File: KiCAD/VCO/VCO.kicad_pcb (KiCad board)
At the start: 4 copper layers, 215 x 85 mm, 40 parts, among them J1 CV IN 1, J2 CV IN 2, J3 PWM, J4 SAW OUT, J5 PULSE OUT, J6 Conn_01x03_Pin, J7 Conn_01x03_Pin, Q1 NPN, T1 PNP, T2 NPN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

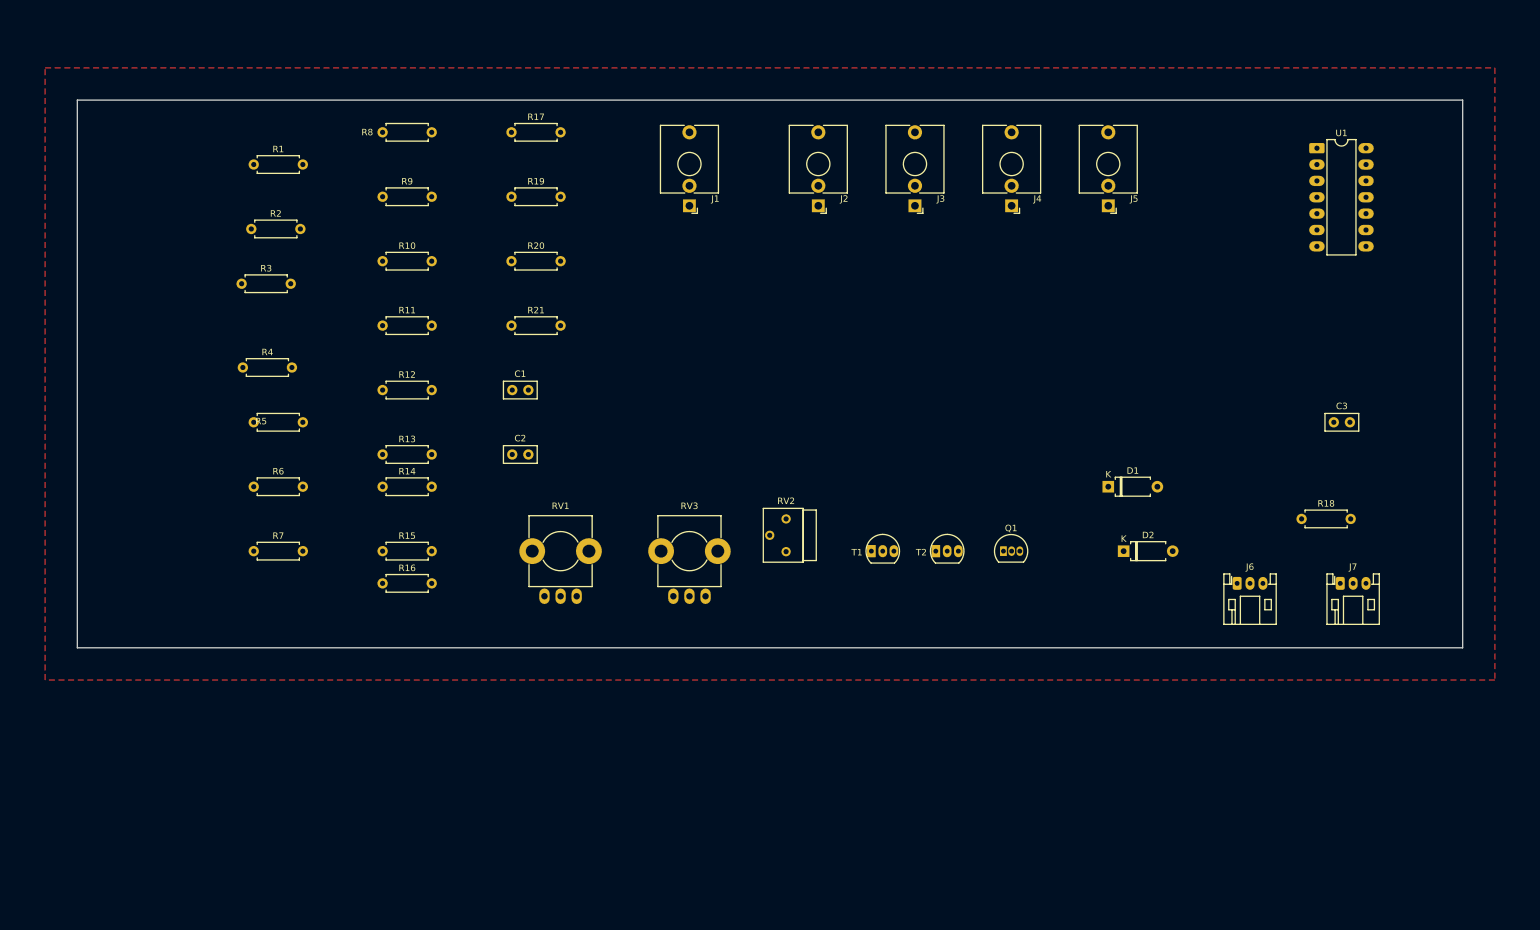
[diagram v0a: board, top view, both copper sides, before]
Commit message: VCO Board Setup
Set up net classes and removed additional layers
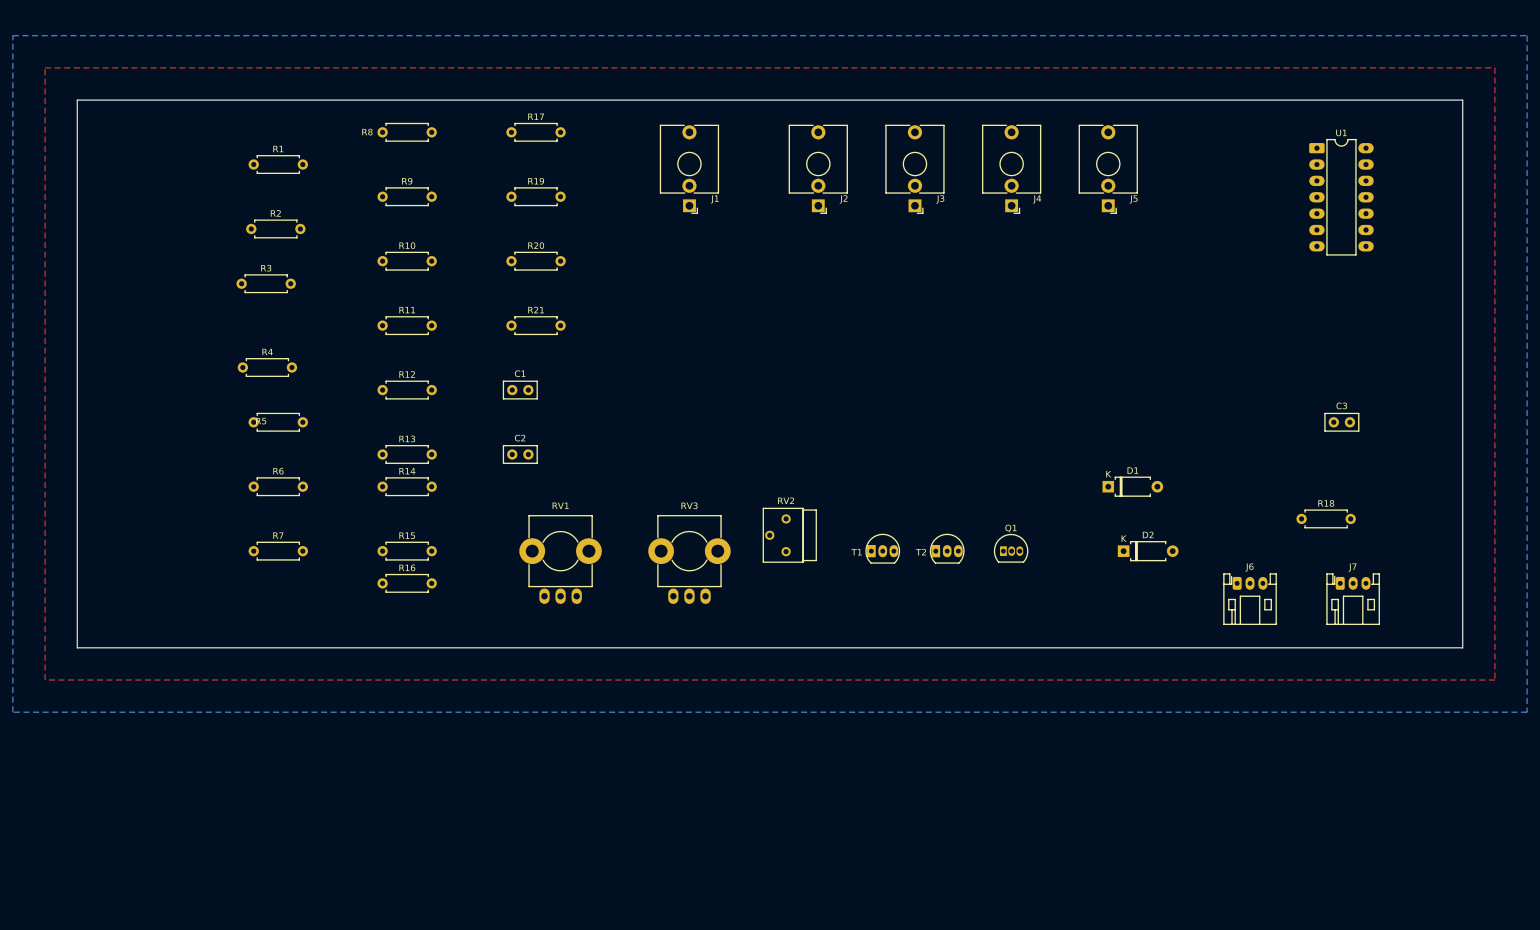
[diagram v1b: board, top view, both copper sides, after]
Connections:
- U1 pad 14: (no net) -> VDD
- U1 pad 7: (no net) -> VSS
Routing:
- added copper zone on B.Cu, net VDD
- removed copper zone on In1.Cu, net VDD
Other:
- copper layers 4 -> 2
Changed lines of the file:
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@@
 	(layers
 		(0 "F.Cu" signal)
-		(4 "In1.Cu" signal)
-		(6 "In2.Cu" signal)
 		(2 "B.Cu" signal)
 		(9 "F.Adhes" user "F.Adhesive")
@@
 			)
 			(layer "dielectric 1"
-				(type "prepreg")
-				(thickness 0.1)
-				(material "FR4")
-				(epsilon_r 4.5)
-				(loss_tangent 0.02)
-			)
-			(layer "In1.Cu"
-				(type "copper")
-				(thickness 0.035)
-			)
-			(layer "dielectric 2"
 				(type "core")
-				(thickness 1.24)
-				(material "FR4")
-				(epsilon_r 4.5)
-				(loss_tangent 0.02)
-			)
-			(layer "In2.Cu"
-				(type "copper")
-				(thickness 0.035)
-			)
-			(layer "dielectric 3"
-				(type "prepreg")
-				(thickness 0.1)
+				(thickness 1.51)
 				(material "FR4")
 				(epsilon_r 4.5)
@@
 			(psa4output no)
 			(plot_black_and_white yes)
-			(plotinvisibletext no)
 			(sketchpadsonfab no)
 			(plotpadnumbers no)
@@
 			(net 0)
 			(net_name "")
-			(layers "F.Cu" "In1.Cu" "In2.Cu")
+			(layer "F.Cu")
 			(hatch full 0.508)
 			(connect_pads
@@
 			(net 0)
 			(net_name "")
-			(layers "F.Cu" "In1.Cu" "In2.Cu")
+			(layer "F.Cu")
 			(hatch full 0.508)
 			(connect_pads
@@
 			(layers "*.Cu" "*.Mask")
 			(remove_unused_layers no)
+			(net 27 "VSS")
 		)
 		(pad "8" thru_hole oval
@@
 			(layers "*.Cu" "*.Mask")
 			(remove_unused_layers no)
+			(net 17 "VDD")
 		)
 		(embedded_fonts no)
@@
 			(net 0)
 			(net_name "")
-			(layers "F.Cu" "In1.Cu" "In2.Cu")
+			(layer "F.Cu")
 			(hatch full 0.508)
 			(connect_pads
@@
 			(net 0)
 			(net_name "")
-			(layers "F.Cu" "In1.Cu" "In2.Cu")
+			(layer "F.Cu")
 			(hatch full 0.508)
 			(connect_pads
@@
 			(net 0)
 			(net_name "")
-			(layers "F.Cu" "In1.Cu" "In2.Cu")
+			(layer "F.Cu")
 			(hatch full 0.508)
 			(connect_pads
@@
 		(net 17)
 		(net_name "VDD")
-		(layer "In1.Cu")
+		(layer "B.Cu")
 		(hatch edge 0.5)
 		(priority 1)

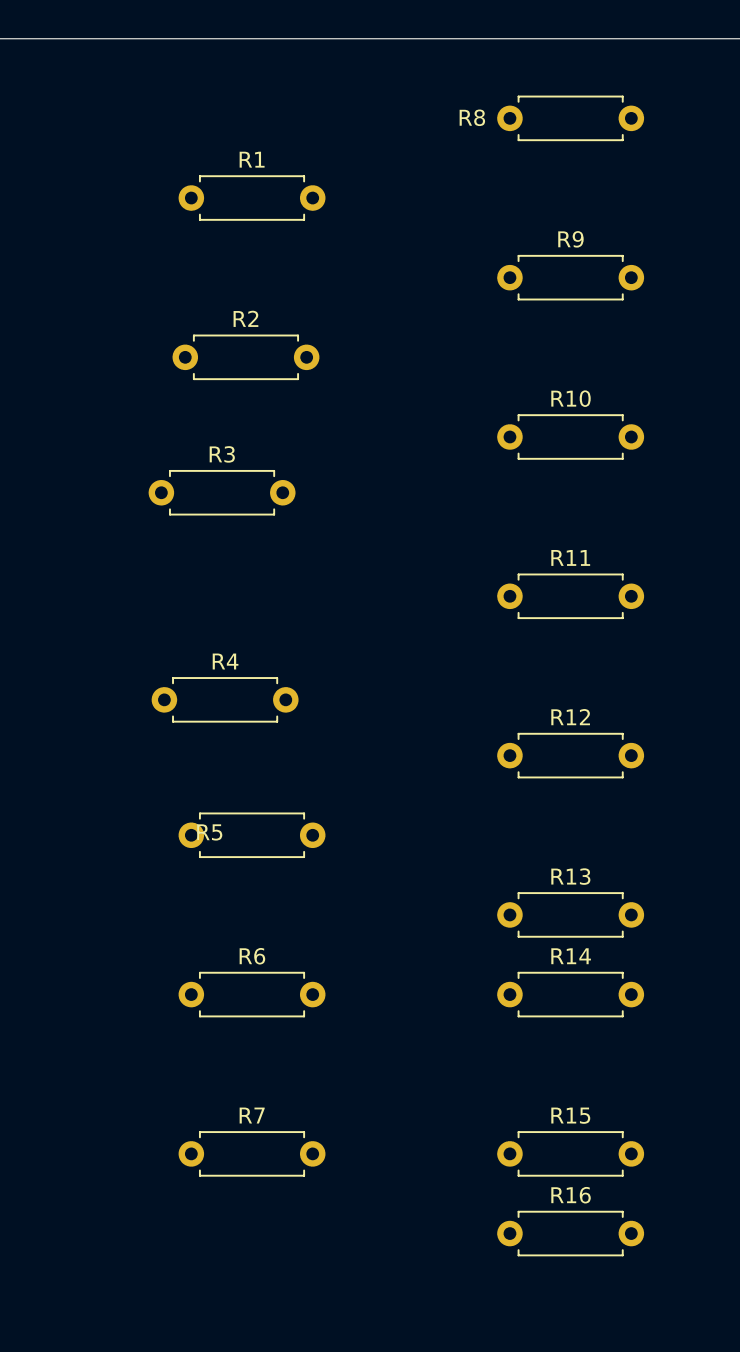
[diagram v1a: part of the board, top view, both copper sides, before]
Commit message: VCO PCB Resistor alignment.
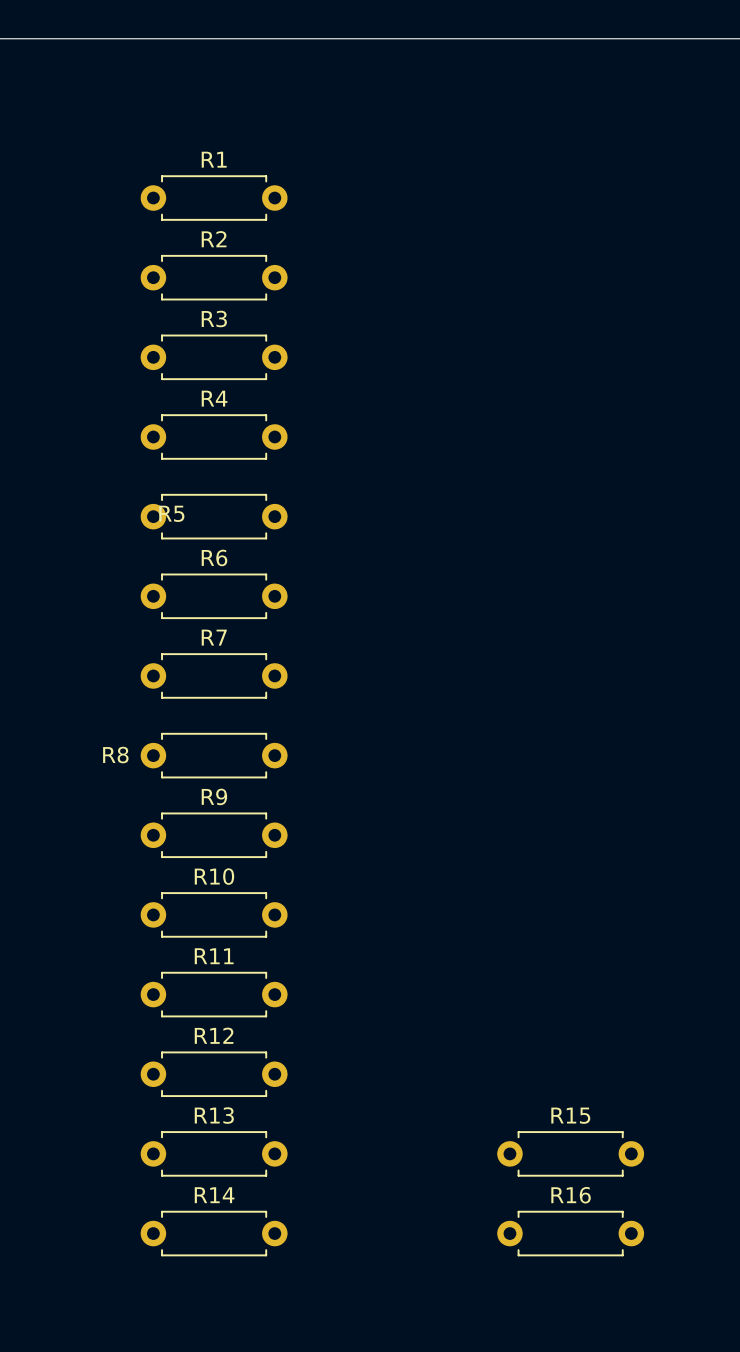
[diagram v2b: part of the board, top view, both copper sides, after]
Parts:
- moved R8 45.8 mm to (60.0, 85.0)
- moved R9 41.5 mm to (60.0, 90.0)
- moved R10 37.4 mm to (60.0, 95.0)
- moved R11 33.6 mm to (60.0, 100.0)
- moved R7 30.1 mm to (60.0, 80.0)
- moved R12 30.0 mm to (60.0, 105.0)
- moved R13 26.9 mm to (60.0, 110.0)
- moved R14 26.9 mm to (60.0, 115.0)
- moved R6 25.1 mm to (60.0, 75.0)
- moved R5 20.1 mm to (60.0, 70.0)
- moved R4 16.5 mm to (60.0, 65.0)
- moved R3 8.51 mm to (60.0, 60.0)
- moved R2 5.39 mm to (60.0, 55.0)
- moved R1 2.38 mm to (60.0, 50.0)
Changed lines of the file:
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@@
 	(footprint "Resistor_THT:R_Axial_DIN0207_L6.3mm_D2.5mm_P7.62mm_Horizontal"
 		(layer "F.Cu")
-		(at 62.38 110)
+		(at 60 80)
 		(descr "Resistor, Axial_DIN0207 series, Axial, Horizontal, pin pitch=7.62mm, 0.25W = 1/4W, length*diameter=6.3*2.5mm^2, http://cdn-reichelt.de/documents/datenblatt/B400/1_4W%23YAG.pdf")
 		(tags "Resistor Axial_DIN0207 series Axial Horizontal pin pitch 7.62mm 0.25W = 1/4W length 6.3mm diameter 2.5mm")
@@
 	(footprint "Resistor_THT:R_Axial_DIN0207_L6.3mm_D2.5mm_P7.62mm_Horizontal"
 		(layer "F.Cu")
-		(at 60.5 68.5)
+		(at 60 60)
 		(descr "Resistor, Axial_DIN0207 series, Axial, Horizontal, pin pitch=7.62mm, 0.25W = 1/4W, length*diameter=6.3*2.5mm^2, http://cdn-reichelt.de/documents/datenblatt/B400/1_4W%23YAG.pdf")
 		(tags "Resistor Axial_DIN0207 series Axial Horizontal pin pitch 7.62mm 0.25W = 1/4W length 6.3mm diameter 2.5mm")
@@
 	(footprint "Resistor_THT:R_Axial_DIN0207_L6.3mm_D2.5mm_P7.62mm_Horizontal"
 		(layer "F.Cu")
-		(at 62.38 90)
+		(at 60 70)
 		(descr "Resistor, Axial_DIN0207 series, Axial, Horizontal, pin pitch=7.62mm, 0.25W = 1/4W, length*diameter=6.3*2.5mm^2, http://cdn-reichelt.de/documents/datenblatt/B400/1_4W%23YAG.pdf")
 		(tags "Resistor Axial_DIN0207 series Axial Horizontal pin pitch 7.62mm 0.25W = 1/4W length 6.3mm diameter 2.5mm")
@@
 	(footprint "Resistor_THT:R_Axial_DIN0207_L6.3mm_D2.5mm_P7.62mm_Horizontal"
 		(layer "F.Cu")
-		(at 82.38 75)
+		(at 60 100)
 		(descr "Resistor, Axial_DIN0207 series, Axial, Horizontal, pin pitch=7.62mm, 0.25W = 1/4W, length*diameter=6.3*2.5mm^2, http://cdn-reichelt.de/documents/datenblatt/B400/1_4W%23YAG.pdf")
 		(tags "Resistor Axial_DIN0207 series Axial Horizontal pin pitch 7.62mm 0.25W = 1/4W length 6.3mm diameter 2.5mm")
@@
 	(footprint "Resistor_THT:R_Axial_DIN0207_L6.3mm_D2.5mm_P7.62mm_Horizontal"
 		(layer "F.Cu")
-		(at 82.38 85)
+		(at 60 105)
 		(descr "Resistor, Axial_DIN0207 series, Axial, Horizontal, pin pitch=7.62mm, 0.25W = 1/4W, length*diameter=6.3*2.5mm^2, http://cdn-reichelt.de/documents/datenblatt/B400/1_4W%23YAG.pdf")
 		(tags "Resistor Axial_DIN0207 series Axial Horizontal pin pitch 7.62mm 0.25W = 1/4W length 6.3mm diameter 2.5mm")
@@
 	(footprint "Resistor_THT:R_Axial_DIN0207_L6.3mm_D2.5mm_P7.62mm_Horizontal"
 		(layer "F.Cu")
-		(at 82.38 45)
+		(at 60 85)
 		(descr "Resistor, Axial_DIN0207 series, Axial, Horizontal, pin pitch=7.62mm, 0.25W = 1/4W, length*diameter=6.3*2.5mm^2, http://cdn-reichelt.de/documents/datenblatt/B400/1_4W%23YAG.pdf")
 		(tags "Resistor Axial_DIN0207 series Axial Horizontal pin pitch 7.62mm 0.25W = 1/4W length 6.3mm diameter 2.5mm")
@@
 	(footprint "Resistor_THT:R_Axial_DIN0207_L6.3mm_D2.5mm_P7.62mm_Horizontal"
 		(layer "F.Cu")
-		(at 82.38 95)
+		(at 60 110)
 		(descr "Resistor, Axial_DIN0207 series, Axial, Horizontal, pin pitch=7.62mm, 0.25W = 1/4W, length*diameter=6.3*2.5mm^2, http://cdn-reichelt.de/documents/datenblatt/B400/1_4W%23YAG.pdf")
 		(tags "Resistor Axial_DIN0207 series Axial Horizontal pin pitch 7.62mm 0.25W = 1/4W length 6.3mm diameter 2.5mm")
@@
 	(footprint "Resistor_THT:R_Axial_DIN0207_L6.3mm_D2.5mm_P7.62mm_Horizontal"
 		(layer "F.Cu")
-		(at 82.38 100)
+		(at 60 115)
 		(descr "Resistor, Axial_DIN0207 series, Axial, Horizontal, pin pitch=7.62mm, 0.25W = 1/4W, length*diameter=6.3*2.5mm^2, http://cdn-reichelt.de/documents/datenblatt/B400/1_4W%23YAG.pdf")
 		(tags "Resistor Axial_DIN0207 series Axial Horizontal pin pitch 7.62mm 0.25W = 1/4W length 6.3mm diameter 2.5mm")
@@
 	(footprint "Resistor_THT:R_Axial_DIN0207_L6.3mm_D2.5mm_P7.62mm_Horizontal"
 		(layer "F.Cu")
-		(at 62 60)
+		(at 60 55)
 		(descr "Resistor, Axial_DIN0207 series, Axial, Horizontal, pin pitch=7.62mm, 0.25W = 1/4W, length*diameter=6.3*2.5mm^2, http://cdn-reichelt.de/documents/datenblatt/B400/1_4W%23YAG.pdf")
 		(tags "Resistor Axial_DIN0207 series Axial Horizontal pin pitch 7.62mm 0.25W = 1/4W length 6.3mm diameter 2.5mm")
@@
 	(footprint "Resistor_THT:R_Axial_DIN0207_L6.3mm_D2.5mm_P7.62mm_Horizontal"
 		(layer "F.Cu")
-		(at 82.38 55)
+		(at 60 90)
 		(descr "Resistor, Axial_DIN0207 series, Axial, Horizontal, pin pitch=7.62mm, 0.25W = 1/4W, length*diameter=6.3*2.5mm^2, http://cdn-reichelt.de/documents/datenblatt/B400/1_4W%23YAG.pdf")
 		(tags "Resistor Axial_DIN0207 series Axial Horizontal pin pitch 7.62mm 0.25W = 1/4W length 6.3mm diameter 2.5mm")
@@
 	(footprint "Resistor_THT:R_Axial_DIN0207_L6.3mm_D2.5mm_P7.62mm_Horizontal"
 		(layer "F.Cu")
-		(at 60.69 81.5)
+		(at 60 65)
 		(descr "Resistor, Axial_DIN0207 series, Axial, Horizontal, pin pitch=7.62mm, 0.25W = 1/4W, length*diameter=6.3*2.5mm^2, http://cdn-reichelt.de/documents/datenblatt/B400/1_4W%23YAG.pdf")
 		(tags "Resistor Axial_DIN0207 series Axial Horizontal pin pitch 7.62mm 0.25W = 1/4W length 6.3mm diameter 2.5mm")
@@
 	(footprint "Resistor_THT:R_Axial_DIN0207_L6.3mm_D2.5mm_P7.62mm_Horizontal"
 		(layer "F.Cu")
-		(at 62.38 50)
+		(at 60 50)
 		(descr "Resistor, Axial_DIN0207 series, Axial, Horizontal, pin pitch=7.62mm, 0.25W = 1/4W, length*diameter=6.3*2.5mm^2, http://cdn-reichelt.de/documents/datenblatt/B400/1_4W%23YAG.pdf")
 		(tags "Resistor Axial_DIN0207 series Axial Horizontal pin pitch 7.62mm 0.25W = 1/4W length 6.3mm diameter 2.5mm")
@@
 	(footprint "Resistor_THT:R_Axial_DIN0207_L6.3mm_D2.5mm_P7.62mm_Horizontal"
 		(layer "F.Cu")
-		(at 82.38 65)
+		(at 60 95)
 		(descr "Resistor, Axial_DIN0207 series, Axial, Horizontal, pin pitch=7.62mm, 0.25W = 1/4W, length*diameter=6.3*2.5mm^2, http://cdn-reichelt.de/documents/datenblatt/B400/1_4W%23YAG.pdf")
 		(tags "Resistor Axial_DIN0207 series Axial Horizontal pin pitch 7.62mm 0.25W = 1/4W length 6.3mm diameter 2.5mm")
@@
 	(footprint "Resistor_THT:R_Axial_DIN0207_L6.3mm_D2.5mm_P7.62mm_Horizontal"
 		(layer "F.Cu")
-		(at 62.38 100)
+		(at 60 75)
 		(descr "Resistor, Axial_DIN0207 series, Axial, Horizontal, pin pitch=7.62mm, 0.25W = 1/4W, length*diameter=6.3*2.5mm^2, http://cdn-reichelt.de/documents/datenblatt/B400/1_4W%23YAG.pdf")
 		(tags "Resistor Axial_DIN0207 series Axial Horizontal pin pitch 7.62mm 0.25W = 1/4W length 6.3mm diameter 2.5mm")
